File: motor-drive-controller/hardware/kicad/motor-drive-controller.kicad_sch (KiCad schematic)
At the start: 0 parts

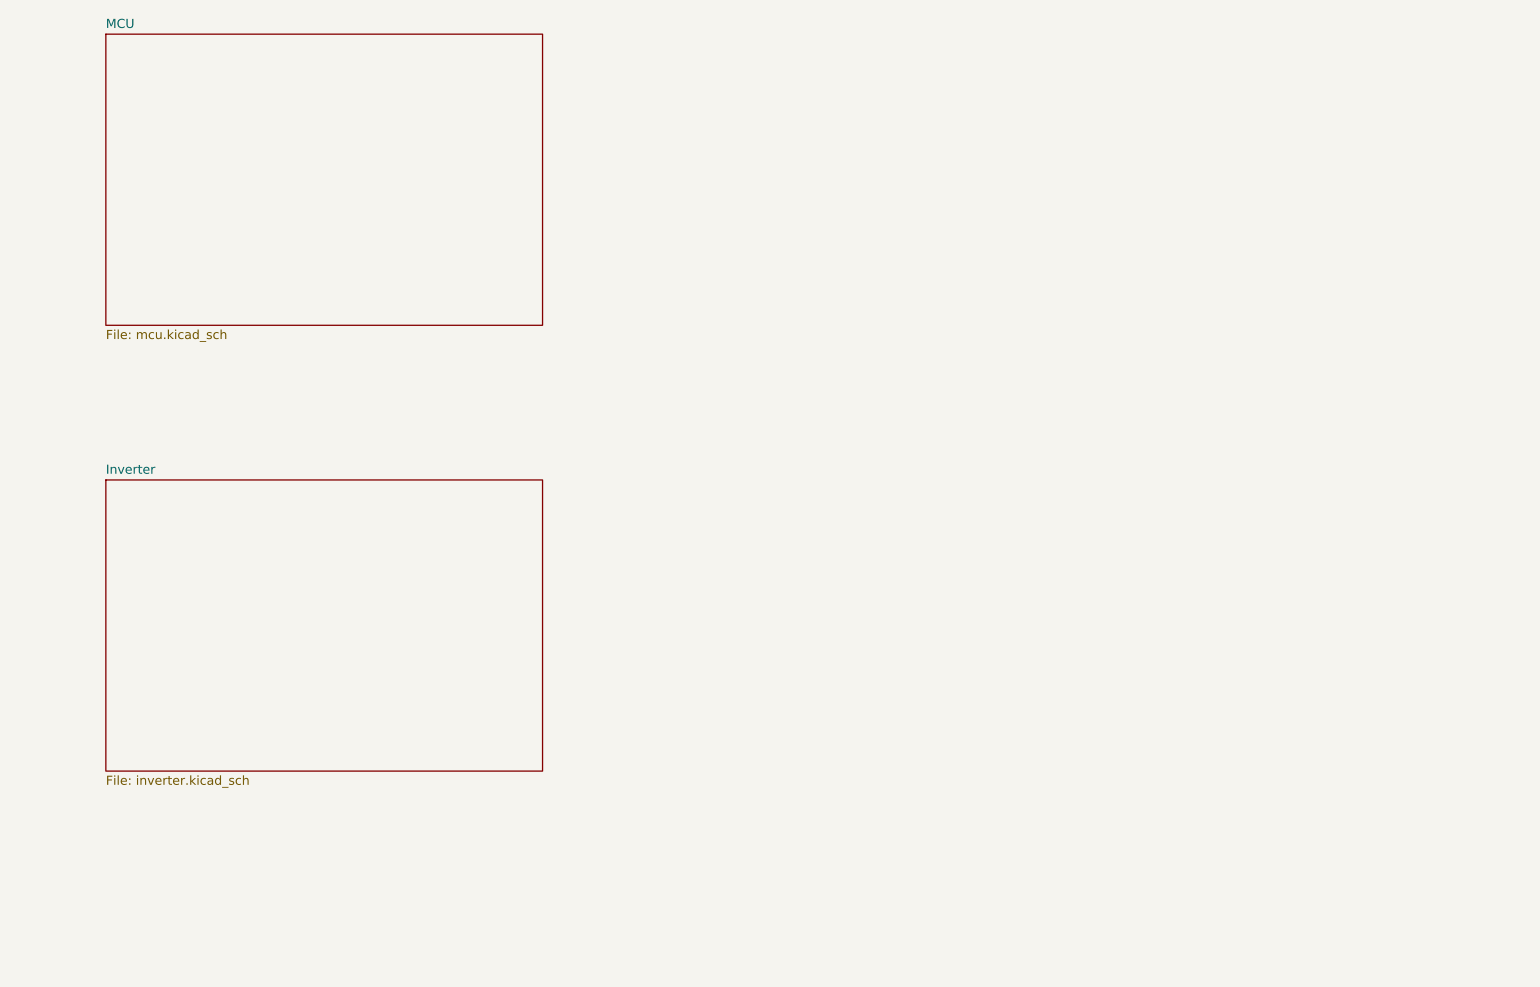
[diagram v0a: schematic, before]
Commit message: hw08(gate-driver): add gate driver sheet and configure MCU
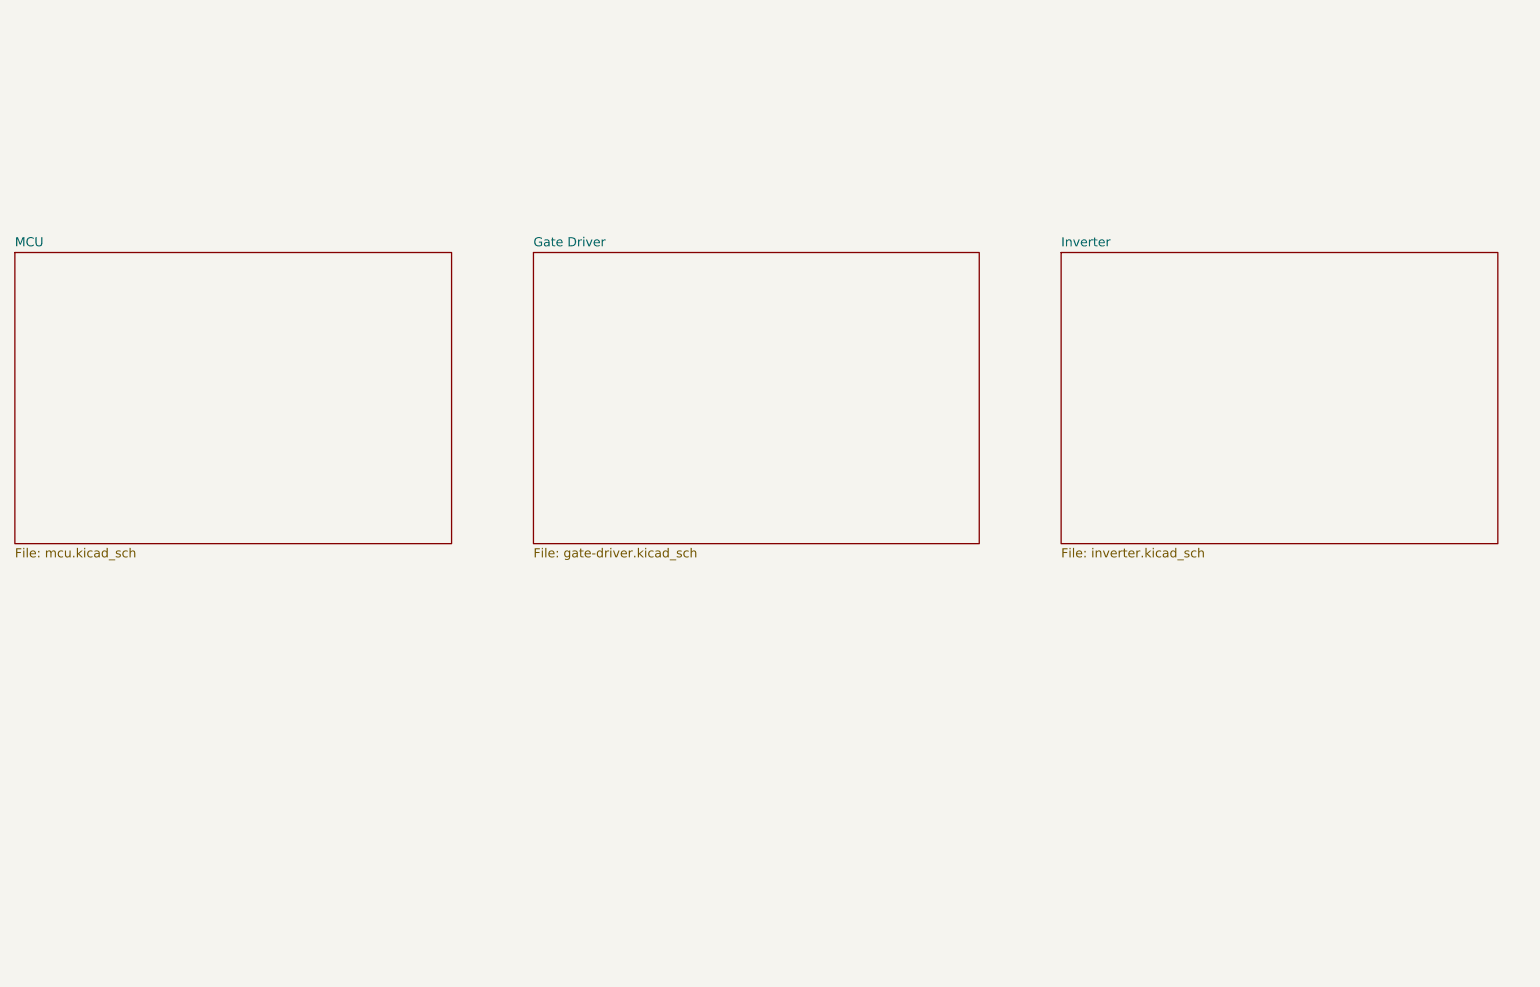
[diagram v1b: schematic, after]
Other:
- added sheet Gate Driver (gate-driver.kicad_sch)
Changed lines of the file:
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@@
 	)
 	(sheet
-		(at 45.72 39.37)
+		(at 105.41 69.85)
+		(size 62.23 40.64)
+		(exclude_from_sim no)
+		(in_bom yes)
+		(on_board yes)
+		(dnp no)
+		(fields_autoplaced yes)
+		(stroke
+			(width 0.1524)
+			(type solid)
+		)
+		(fill
+			(color 0 0 0 0)
+		)
+		(property "Sheetname" "Gate Driver"
+			(at 105.41 69.1384 0)
+			(show_name no)
+			(do_not_autoplace no)
+			(effects
+				(font
+					(size 1.27 1.27)
+				)
+				(justify left bottom)
+			)
+		)
+		(property "Sheetfile" "gate-driver.kicad_sch"
+			(at 105.41 111.0746 0)
+			(show_name no)
+			(do_not_autoplace no)
+			(effects
+				(font
+					(size 1.27 1.27)
+				)
+				(justify left top)
+			)
+		)
+		(instances
+			(project "motor-drive-controller"
+				(path "/b8e0307a-d356-4cd3-91c6-dd251b6e910b"
+					(page "3")
+				)
+			)
+		)
+	)
+	(sheet
+		(at 33.02 69.85)
 		(size 60.96 40.64)
 		(exclude_from_sim no)
@@
 		)
 		(property "Sheetname" "MCU"
-			(at 45.72 38.6584 0)
+			(at 33.02 69.1384 0)
 			(show_name no)
 			(do_not_autoplace no)
@@
 		)
 		(property "Sheetfile" "mcu.kicad_sch"
-			(at 45.72 80.5946 0)
+			(at 33.02 111.0746 0)
 			(show_name no)
 			(do_not_autoplace no)
@@
 	)
 	(sheet
-		(at 45.72 101.6)
+		(at 179.07 69.85)
 		(size 60.96 40.64)
 		(exclude_from_sim no)
@@
 		)
 		(property "Sheetname" "Inverter"
-			(at 45.72 100.8884 0)
+			(at 179.07 69.1384 0)
 			(show_name no)
 			(do_not_autoplace no)
@@
 		)
 		(property "Sheetfile" "inverter.kicad_sch"
-			(at 45.72 142.8246 0)
+			(at 179.07 111.0746 0)
 			(show_name no)
 			(do_not_autoplace no)
@@
 			(project "motor-drive-controller"
 				(path "/b8e0307a-d356-4cd3-91c6-dd251b6e910b"
-					(page "3")
+					(page "4")
 				)
 			)

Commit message: feat(hw09): create links between labels of different hierarchical sheets
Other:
- sheet Gate Driver ports: added CS{SHUNT6}, DRV{PWM6}, DRV{SPI}, DRV{STATUS}, GATE{GATE6}, PH{SENSE6}; removed none
- sheet Inverter ports: added CS{SHUNT6}, GATE{GATE6}, PH{SENSE6}, TEMP_SENSE; removed none
- sheet MCU ports: added DRV{PWM6}, DRV{SPI}, DRV{STATUS}, TEMP_SENSE; removed none

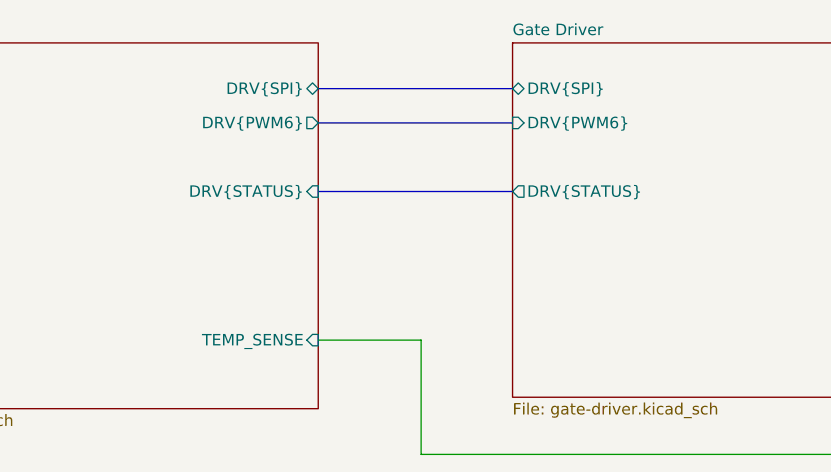
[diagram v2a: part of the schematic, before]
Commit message: feat(hw09): add ISENSE ADC channels and update schematics
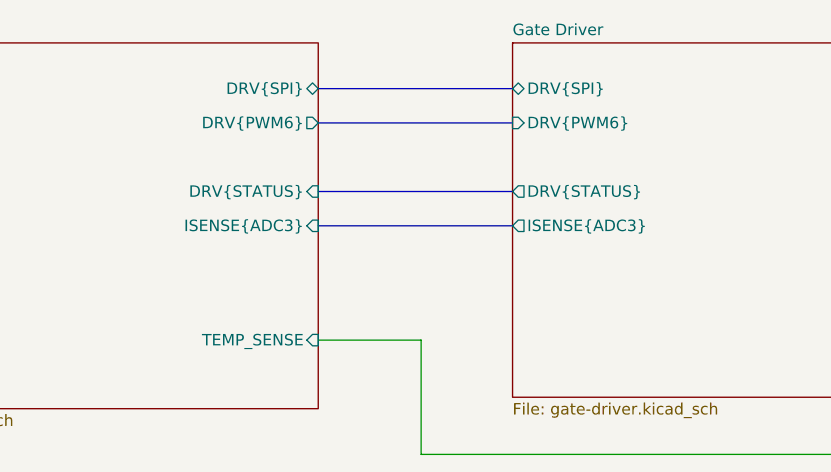
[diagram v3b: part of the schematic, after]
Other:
- sheet Gate Driver ports: added ISENSE{ADC3}; removed none
- sheet MCU ports: added ISENSE{ADC3}; removed none
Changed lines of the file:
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@@
+		)
+	)
+	(bus
+		(pts
+			(xy 95.25 87.63) (xy 116.84 87.63)
+		)
+		(stroke
+			(width 0)
+			(type default)
 		)
 	)
@@
 			)
 		)
+		(pin "ISENSE{ADC3}" output
+			(at 116.84 87.63 180)
+			(effects
+				(font
+					(size 1.27 1.27)
+				)
+				(justify left)
+			)
+		)
 		(instances
 			(project "motor-drive-controller"
@@
 			(effects
 				(font
+					(size 1.27 1.27)
+				)
+				(justify right)
+			)
+		)
+		(pin "ISENSE{ADC3}" input
+			(at 95.25 87.63 0)
+			(effects
+				(font

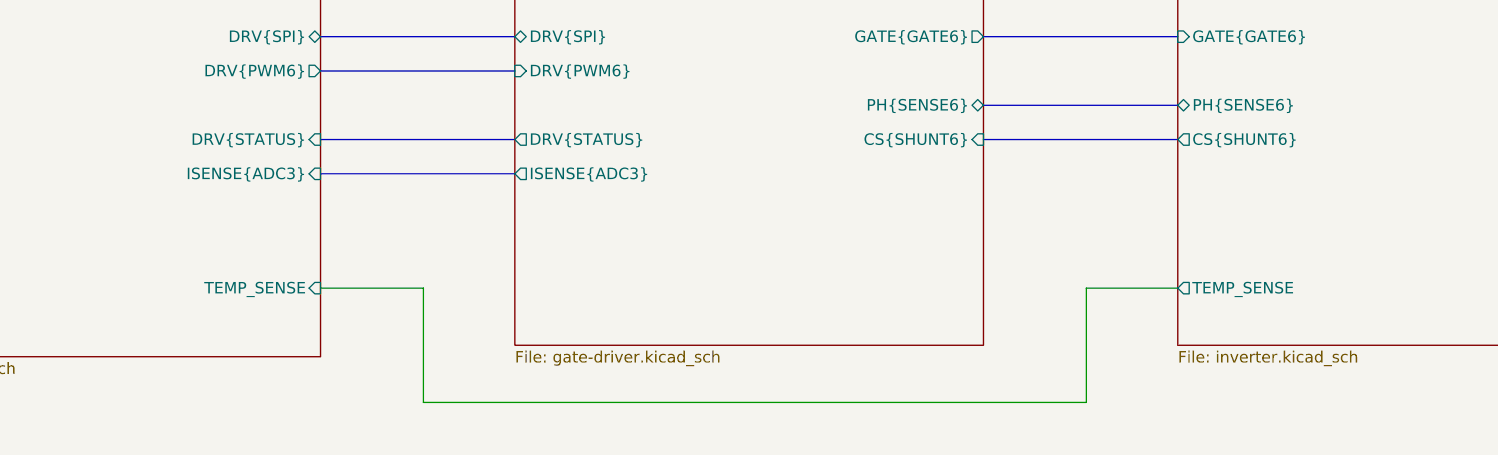
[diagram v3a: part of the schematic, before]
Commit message: feat(hw09): update ADC channel names and schematic references to ANALOG prefix
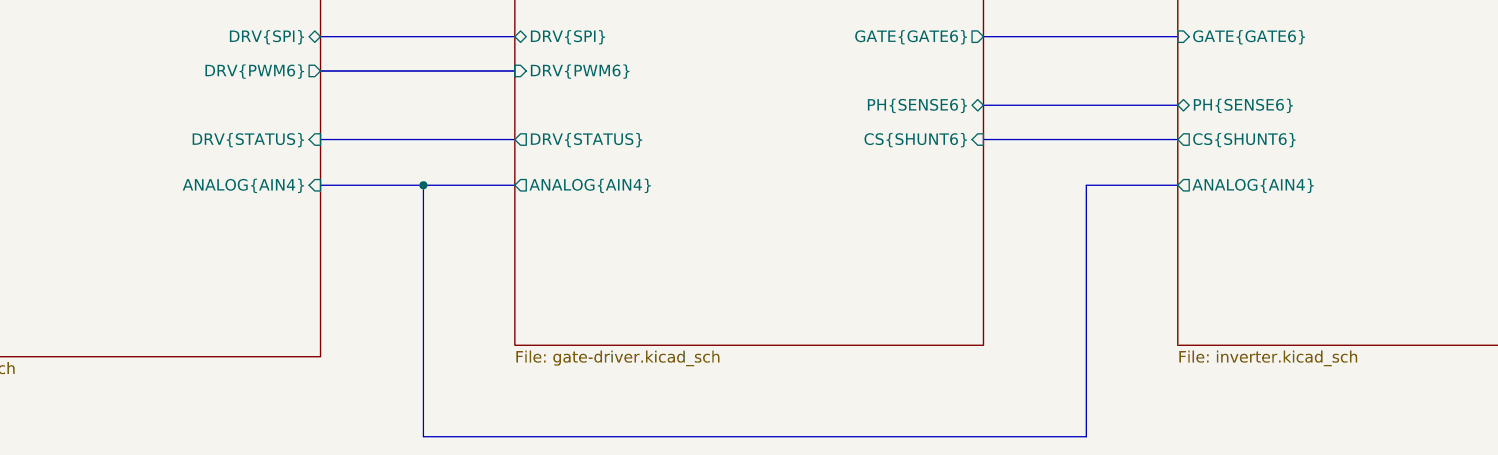
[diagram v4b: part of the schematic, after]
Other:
- sheet Gate Driver ports: added ANALOG{AIN4}; removed ISENSE{ADC3}
- sheet Inverter ports: added ANALOG{AIN4}; removed TEMP_SENSE
- sheet MCU ports: added ANALOG{AIN4}; removed ISENSE{ADC3}, TEMP_SENSE
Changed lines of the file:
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@@
 		(title "Motor Drive Controller")
 	)
-	(wire
-		(pts
-			(xy 180.34 100.33) (xy 180.34 113.03)
+	(junction
+		(at 106.68 88.9)
+		(diameter 0)
+		(color 0 0 0 0)
+	)
+	(bus
+		(pts
+			(xy 190.5 88.9) (xy 180.34 88.9)
+		)
+		(stroke
+			(width 0)
+			(type default)
+		)
+	)
+	(bus
+		(pts
+			(xy 95.25 88.9) (xy 106.68 88.9)
+		)
+		(stroke
+			(width 0)
+			(type default)
+		)
+	)
+	(bus
+		(pts
+			(xy 180.34 116.84) (xy 106.68 116.84)
 		)
 		(stroke
@@
 		)
 	)
-	(wire
-		(pts
-			(xy 106.68 113.03) (xy 106.68 100.33)
-		)
-		(stroke
-			(width 0)
-			(type default)
-		)
-	)
 	(bus
 		(pts
@@
 		)
 	)
-	(wire
-		(pts
-			(xy 190.5 100.33) (xy 180.34 100.33)
+	(bus
+		(pts
+			(xy 106.68 88.9) (xy 106.68 116.84)
+		)
+		(stroke
+			(width 0)
+			(type default)
+		)
+	)
+	(bus
+		(pts
+			(xy 106.68 88.9) (xy 116.84 88.9)
+		)
+		(stroke
+			(width 0)
+			(type default)
+		)
+	)
+	(bus
+		(pts
+			(xy 180.34 88.9) (xy 180.34 116.84)
 		)
 		(stroke
@@
 		(pts
 			(xy 168.91 72.39) (xy 190.5 72.39)
-		)
-		(stroke
-			(width 0)
-			(type default)
-		)
-	)
-	(bus
-		(pts
-			(xy 95.25 87.63) (xy 116.84 87.63)
-		)
-		(stroke
-			(width 0)
-			(type default)
-		)
-	)
-	(wire
-		(pts
-			(xy 180.34 113.03) (xy 106.68 113.03)
-		)
-		(stroke
-			(width 0)
-			(type default)
-		)
-	)
-	(wire
-		(pts
-			(xy 95.25 100.33) (xy 106.68 100.33)
 		)
 		(stroke
@@
 			)
 		)
-		(pin "ISENSE{ADC3}" output
-			(at 116.84 87.63 180)
+		(pin "ANALOG{AIN4}" output
+			(at 116.84 88.9 180)
 			(effects
 				(font
@@
 			)
 		)
-		(pin "TEMP_SENSE" input
-			(at 95.25 100.33 0)
-			(effects
-				(font
-					(size 1.27 1.27)
-				)
-				(justify right)
-			)
-		)
-		(pin "ISENSE{ADC3}" input
-			(at 95.25 87.63 0)
+		(pin "ANALOG{AIN4}" input
+			(at 95.25 88.9 0)
 			(effects
 				(font
@@
 			)
 		)
-		(pin "TEMP_SENSE" output
-			(at 190.5 100.33 180)
-			(effects
-				(font
+		(pin "ANALOG{AIN4}" output
+			(at 190.5 88.9 180)
+			(effects
+				(font

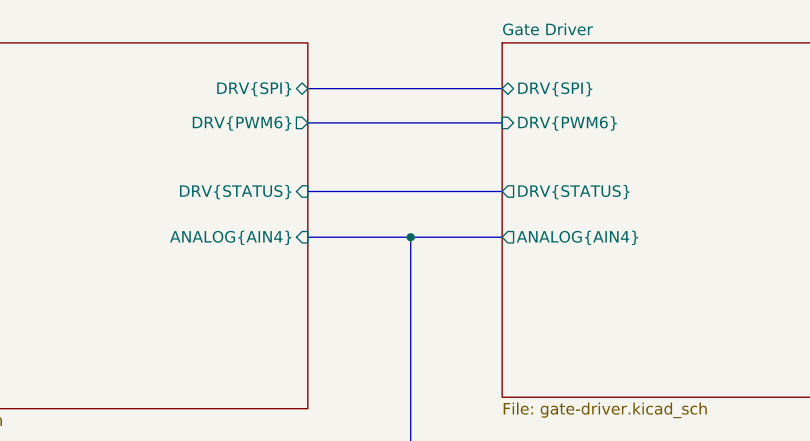
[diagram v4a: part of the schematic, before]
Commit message: feat(hw09): add EN_GATE control and WAKE signal handling in hardware design
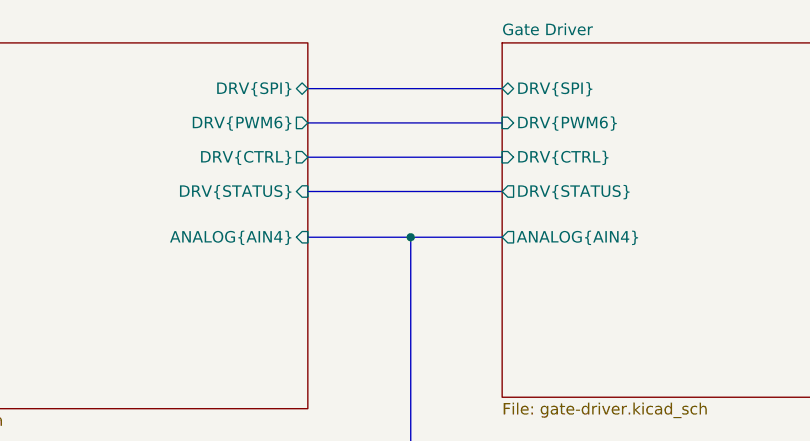
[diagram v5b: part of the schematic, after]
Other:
- sheet Gate Driver ports: added DRV{CTRL}; removed none
- sheet MCU ports: added DRV{CTRL}; removed none
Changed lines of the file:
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@@
+	(bus
+		(pts
+			(xy 95.25 80.01) (xy 116.84 80.01)
+		)
+		(stroke
+			(width 0)
+			(type default)
+		)
+	)
 	(bus
 		(pts
@@
 			)
 		)
+		(pin "DRV{CTRL}" input
+			(at 116.84 80.01 180)
+			(effects
+				(font
+					(size 1.27 1.27)
+				)
+				(justify left)
+			)
+		)
 		(instances
 			(project "motor-drive-controller"
@@
 			(effects
 				(font
+					(size 1.27 1.27)
+				)
+				(justify right)
+			)
+		)
+		(pin "DRV{CTRL}" output
+			(at 95.25 80.01 0)
+			(effects
+				(font

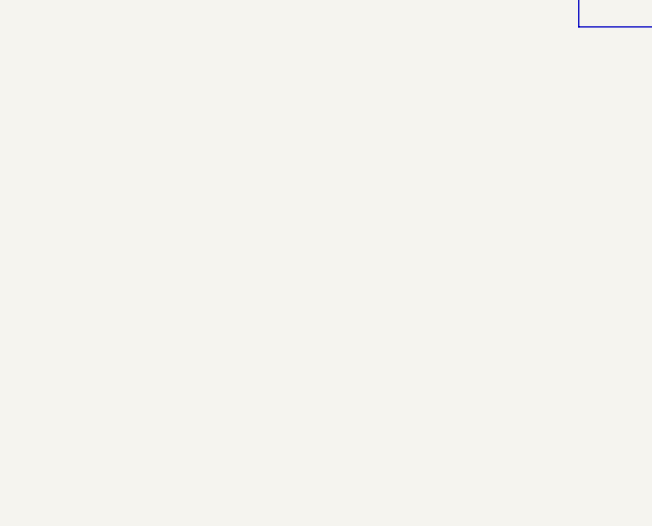
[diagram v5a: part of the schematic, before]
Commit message: feat(hw10): add  power LDO +5V --> +3.3V schema
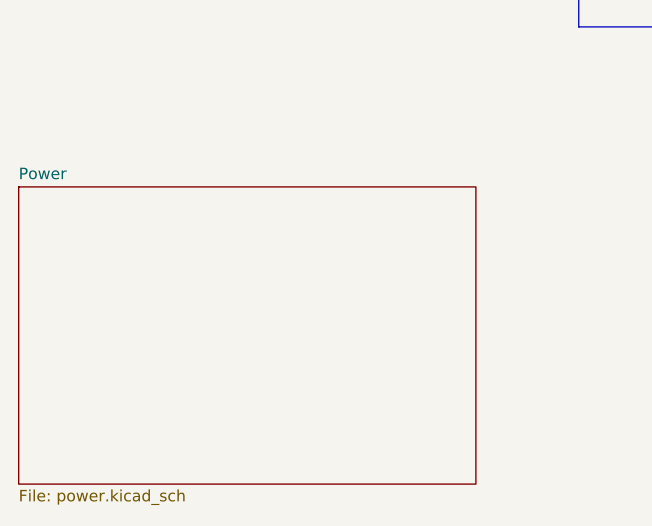
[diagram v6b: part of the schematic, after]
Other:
- added sheet Power (power.kicad_sch)
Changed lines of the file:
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@@
+	)
+	(sheet
+		(at 44.45 134.62)
+		(size 50.8 33.02)
+		(exclude_from_sim no)
+		(in_bom yes)
+		(on_board yes)
+		(dnp no)
+		(fields_autoplaced yes)
+		(stroke
+			(width 0.1524)
+			(type solid)
+		)
+		(fill
+			(color 0 0 0 0)
+		)
+		(property "Sheetname" "Power"
+			(at 44.45 133.9084 0)
+			(show_name no)
+			(do_not_autoplace no)
+			(effects
+				(font
+					(size 1.27 1.27)
+				)
+				(justify left bottom)
+			)
+		)
+		(property "Sheetfile" "power.kicad_sch"
+			(at 44.45 168.2246 0)
+			(show_name no)
+			(do_not_autoplace no)
+			(effects
+				(font
+					(size 1.27 1.27)
+				)
+				(justify left top)
+			)
+		)
+		(instances
+			(project "motor-drive-controller"
+				(path "/b8e0307a-d356-4cd3-91c6-dd251b6e910b"
+					(page "5")
+				)
+			)
+		)
 	)
 	(sheet
